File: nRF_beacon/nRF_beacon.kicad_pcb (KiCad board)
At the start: 4 copper layers, 60 x 90 mm, 54 parts, among them J1 Conn_02x05_Odd_Even, J2 Conn_02x03_Counter_Clockwise, U1 nRF54L15-QFAA, U2 NPM1300-QEAA-R7, U3 MAX98357A, U4 12BHC186P1-GR, X1 32MHz, X2 32.768 kHz

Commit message: Done a lot of work, connected all traces
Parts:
- removed NT1, NT2: Net Tie, Ekse:NetTieSmall
- R3, R4: footprint Resistor_SMD:R_0603_1608Metric -> Resistor_SMD:R_0402_1005Metric
- U2: footprint Ekse:QFN32_5X5_NOR -> Ekse:QFN-32_EP_5x5_Pitch0.5mm
- moved J2 81.7 mm to (157.7, 140.8)
- moved J1 81.0 mm to (167.4, 140.5)
- moved D1 19.3 mm to (162.7, 75.1), turned to 90 degrees
- moved R3 15.3 mm to (164.0, 84.2)
- moved R4 15.3 mm to (162.7, 84.2)
- moved FB2 15.2 mm to (156.3, 111.3), turned to 180 degrees
- moved C20 14.0 mm to (159.5, 112.0)
- moved C14 11.7 mm to (158.9, 75.6)
- moved C23 11.3 mm to (157.8, 78.0)
- moved C22 11.3 mm to (161.5, 83.7), turned to 180 degrees
- moved U2 10.9 mm to (162.1, 79.9)
- moved L5 10.9 mm to (155.3, 80.9)
- moved C16 10.9 mm to (155.5, 82.8)
- moved L6 10.9 mm to (155.8, 78.0)
- moved C25 10.9 mm to (167.5, 80.4)
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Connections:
- net Net-(U2-PVDD) renamed /POWER/VSYS
- C14 pad 2: VSS1 -> GND
- C16 pad 2: VSS2 -> GND
- C23 pad 2: VSS1 -> GND
- C24 pad 2: VSS2 -> GND
- FB2 pad 1: Net-(U3-OUTP) -> /AUDIO/OUTP
- FB3 pad 1: Net-(U3-OUTN) -> /AUDIO/OUTN
- U1 pad 39: /MCU/SDA -> /MCU/SCL
- U1 pad 40: /MCU/SCL -> /MCU/SDA
- U2 pad 2: VSS1 -> GND
- U2 pad 6: VSS2 -> GND
- U3 pad 10: Net-(U3-OUTN) -> /AUDIO/OUTN
- U3 pad 9: Net-(U3-OUTP) -> /AUDIO/OUTP
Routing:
- net VDD_AUDIO: track 7.57 -> 112.5 mm, vias 0 -> 2
- net /P1.10: track 1.64 -> 76.8 mm, vias 0 -> 2
- net /P1.09: track 1.54 -> 65.3 mm, vias 0 -> 2
- net VDD_nRF: track 53.4 -> 116.7 mm
- net /P1.13: track 1.53 -> 61.4 mm, vias 0 -> 2
- net /P1.07: track 0.00 -> 56.3 mm, vias 0 -> 2
- net /P1.14: track 1.66 -> 57.8 mm, vias 0 -> 2
- net /VBAT: track 0.00 -> 55.0 mm
- net /P1.08: track 0.00 -> 54.3 mm, vias 0 -> 2
- net /MCU/~{RESET}: track 0.00 -> 45.6 mm
- net /AUDIO/OUTP: track 0.00 -> 41.8 mm
- net /MCU/SWDCLK: track 0.00 -> 40.8 mm
- net /AUDIO/OUTN: track 0.00 -> 38.4 mm
- net /MCU/SWDIO: track 0.00 -> 36.0 mm
- net /BCLK: track 0.00 -> 23.3 mm, vias 0 -> 2
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- added copper zone on B.Cu, net /POWER/VSYS
- added copper zone on F.Cu, net /POWER/VSYS
- added copper zone on B.Cu, net GND
- added copper zone on In1.Cu, net GND
- added copper zone on In2.Cu, net GND
- added copper zone on F.Cu, net VDD_AUDIO

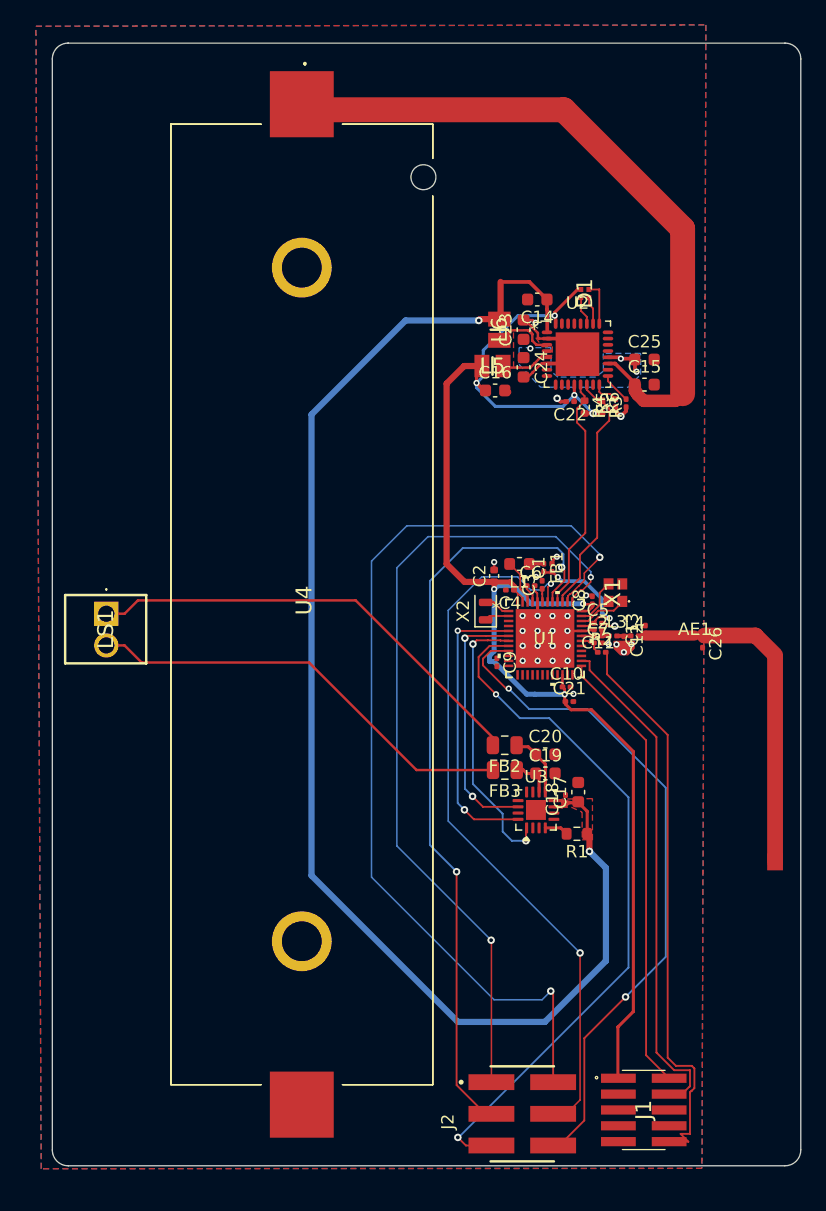
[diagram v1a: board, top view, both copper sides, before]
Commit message: Cleaned up silkscreen
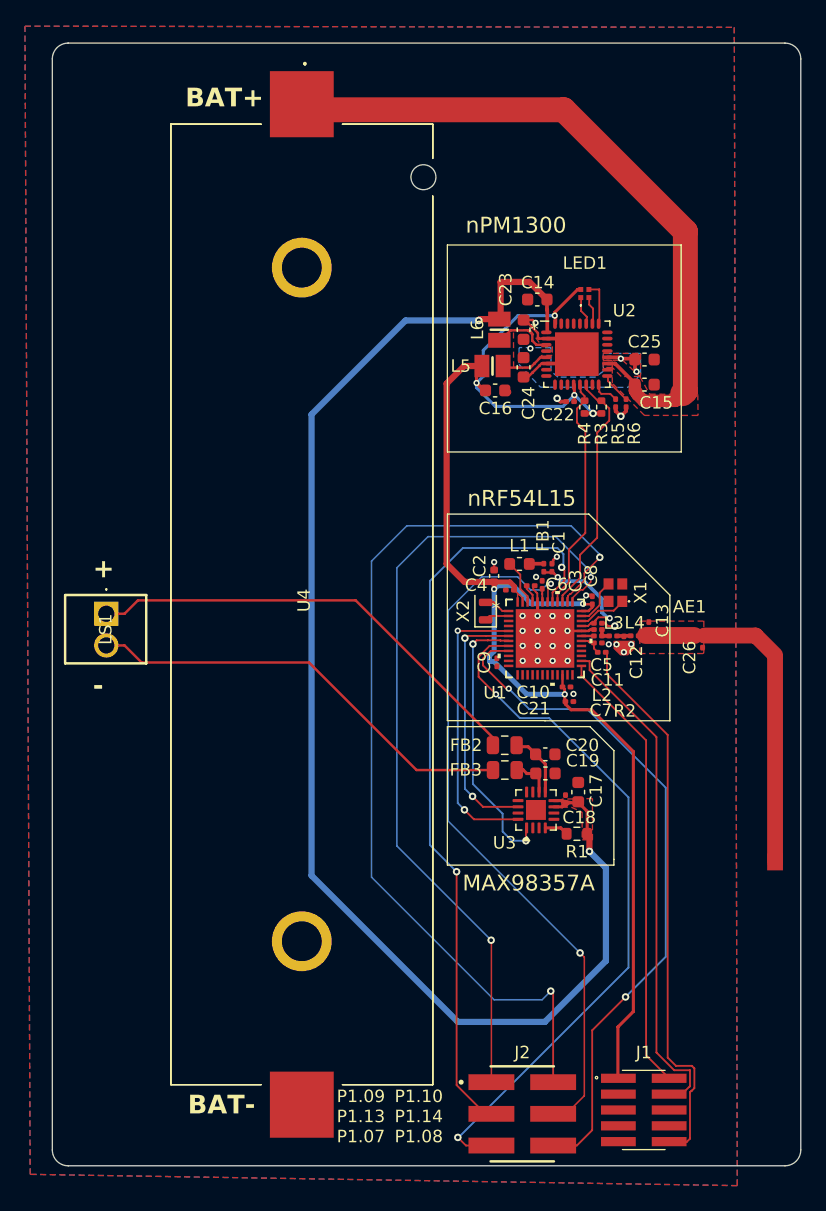
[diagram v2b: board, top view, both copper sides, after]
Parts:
- moved C13 0.40 mm to (167.8, 101.7)
- renumbered D1 to LED1
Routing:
- net /MCU/~{RESET}: track 45.6 -> 44.6 mm
- net /P1.08: track 54.3 -> 55.1 mm
- added copper zone on F.Cu, net /VBAT
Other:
- board text added: "+"
- board text added: "-"
- board text added: "BAT+"
- board text added: "BAT-"
- board text added: "MAX98357A"
- board text added: "P1.09 P1.13 P1.07"
- board text added: "P1.10 P1.14 P1.08"
- board text added: "nPM1300"
- board text added: "nRF54L15"

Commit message: Only 67 DRC errors left
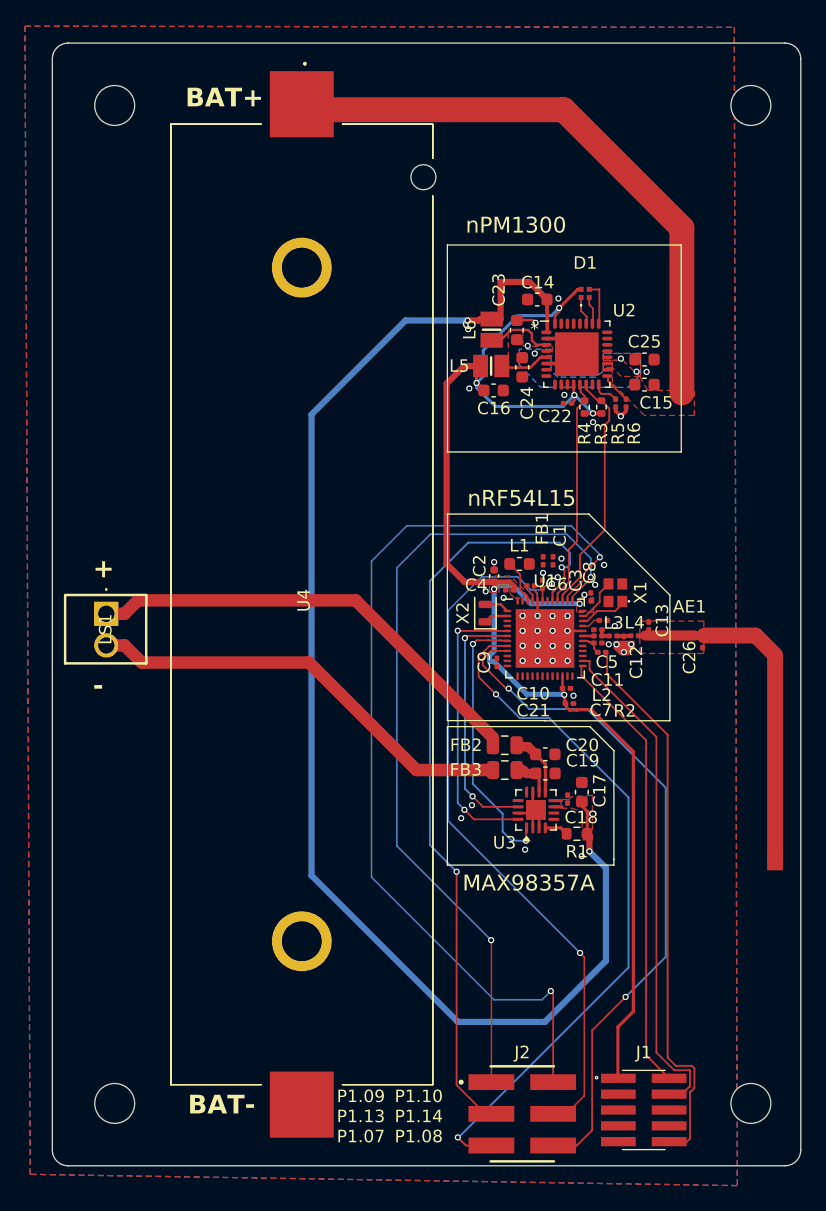
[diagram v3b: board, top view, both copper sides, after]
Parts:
- removed LED1: LED_RGBA, Ekse:APGF1012GBRC07
- added D1: LED_RGBA, Ekse:APGF1012GBRC07, F.Cu at (162.7, 75.1)
- added H1: MountingHole, MountingHole:MountingHole_3.2mm_M3, F.Cu at (125.0, 60.0)
- added H2: MountingHole, MountingHole:MountingHole_3.2mm_M3, F.Cu at (125.0, 140.0)
- added H3: MountingHole, MountingHole:MountingHole_3.2mm_M3, F.Cu at (176.0, 60.0)
- added H4: MountingHole, MountingHole:MountingHole_3.2mm_M3, F.Cu at (176.0, 140.0)
- U1: footprint Ekse:QFN48_6X6_NOR -> Ekse:QFN-48_EP_6x6_Pitch0.4mm
- moved L6 0.62 mm to (155.2, 78.0)
- moved C1 0.56 mm to (160.1, 96.5)
- moved FB1 0.56 mm to (159.3, 96.5)
- moved C23 0.54 mm to (157.2, 78.0)
- moved C5 0.49 mm to (164.2, 101.3)
- moved C8 0.29 mm to (163.2, 99.4)
- moved C17 0.29 mm to (162.4, 115.0)
- moved C22 0.25 mm to (161.3, 83.9)
- moved C18 0.17 mm to (161.3, 115.6)
- moved X2 0.16 mm to (154.7, 100.7)
- moved C21 0.16 mm to (161.4, 107.9)
- moved C16 0.12 mm to (155.4, 82.8)
- moved C10 0.11 mm to (161.2, 106.7)
- moved C24 0.11 mm to (157.7, 81.0)
- moved L5 0.11 mm to (155.2, 80.9)
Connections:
- X1 pad 2: (no net) -> GND
- X1 pad 4: (no net) -> GND
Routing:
- net Net-(U1A-DECA): track 11.1 -> 2.61 mm, vias 2 -> 0
- net /VBAT: track 55.1 -> 47.1 mm
- net GND: track 26.5 -> 23.0 mm, vias 29 -> 44
- net VDD_nRF: track 116.7 -> 113.3 mm
- net /POWER/VSYS: track 3.32 -> 0.21 mm
- net VDD_AUDIO: track 112.5 -> 110.5 mm
- net /P1.13: track 61.4 -> 62.8 mm
- net /P1.14: track 58.1 -> 56.8 mm
- net Net-(U1A-DECD): track 2.68 -> 1.51 mm
- net /P1.09: track 65.3 -> 65.9 mm
- net /MCU/SDA: track 19.0 -> 18.5 mm
- added copper zone on F.Cu, net VDD_nRF

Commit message: Continued fixing DRC errors. Increased trace width on several lines
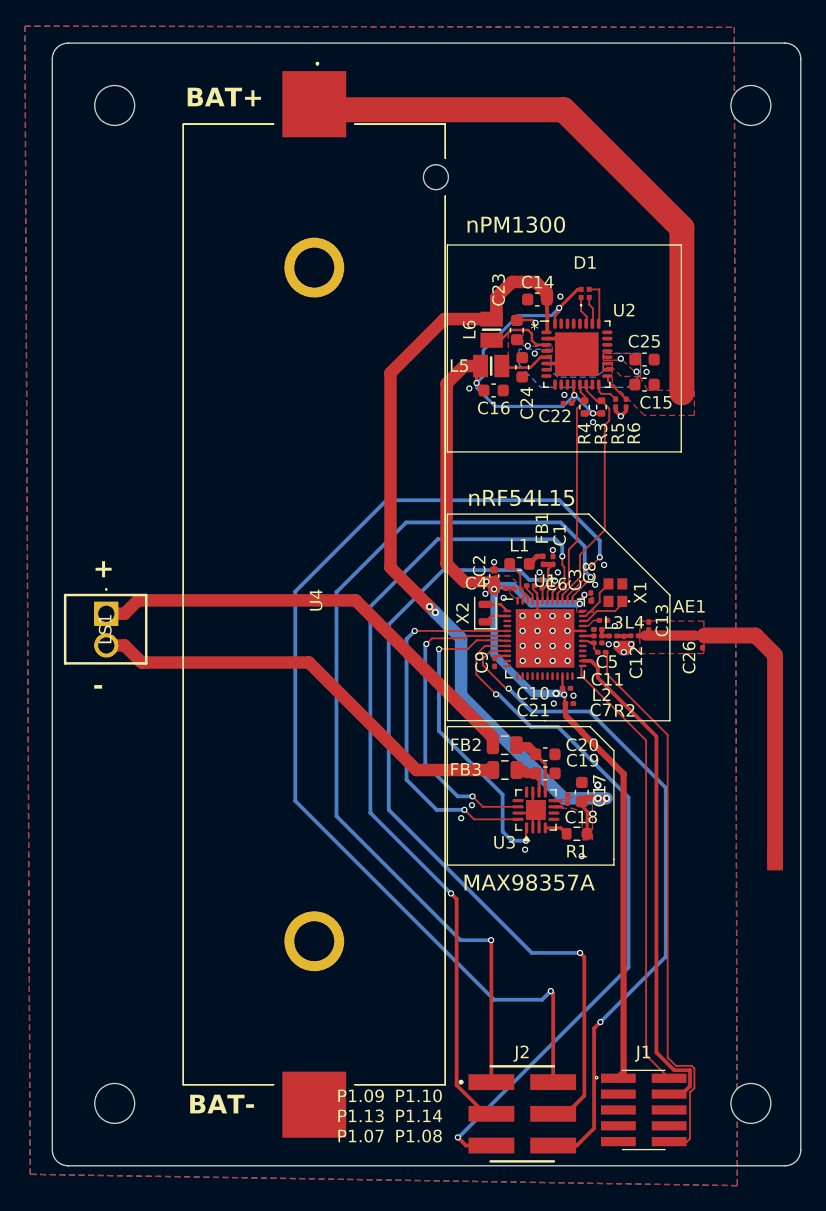
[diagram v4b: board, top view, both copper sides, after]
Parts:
- moved U4 1.00 mm to (141.0, 100.0)
- moved C9 0.18 mm to (155.5, 104.6)
- moved C4 0.12 mm to (156.7, 98.7)
- moved C3 0.06 mm to (159.2, 98.3)
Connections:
- X1 pad 2: GND -> (no net)
- X1 pad 4: GND -> (no net)
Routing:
- net VDD_AUDIO: track 110.5 -> 69.3 mm, vias 2 -> 4
- net /P1.14: track 56.8 -> 67.0 mm
- net /P1.10: track 76.8 -> 86.3 mm
- net /P1.09: track 65.9 -> 74.1 mm
- net /BCLK: track 23.3 -> 30.0 mm
- net /P1.13: track 62.8 -> 67.8 mm
- net /LRCLK: track 20.5 -> 25.4 mm
- net /DIN/DOUT: track 22.2 -> 25.8 mm
- net VDD_nRF: track 113.3 -> 110.1 mm, vias 7 -> 9
- net Net-(U1A-DECA): track 2.61 -> 5.73 mm
- net Net-(U1A-DECD): track 1.51 -> 2.87 mm
- net GND: vias 44 -> 45

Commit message: Adjustments to GPIO connector. Added testpads. Polygon pour by antenna for correct impedance matching
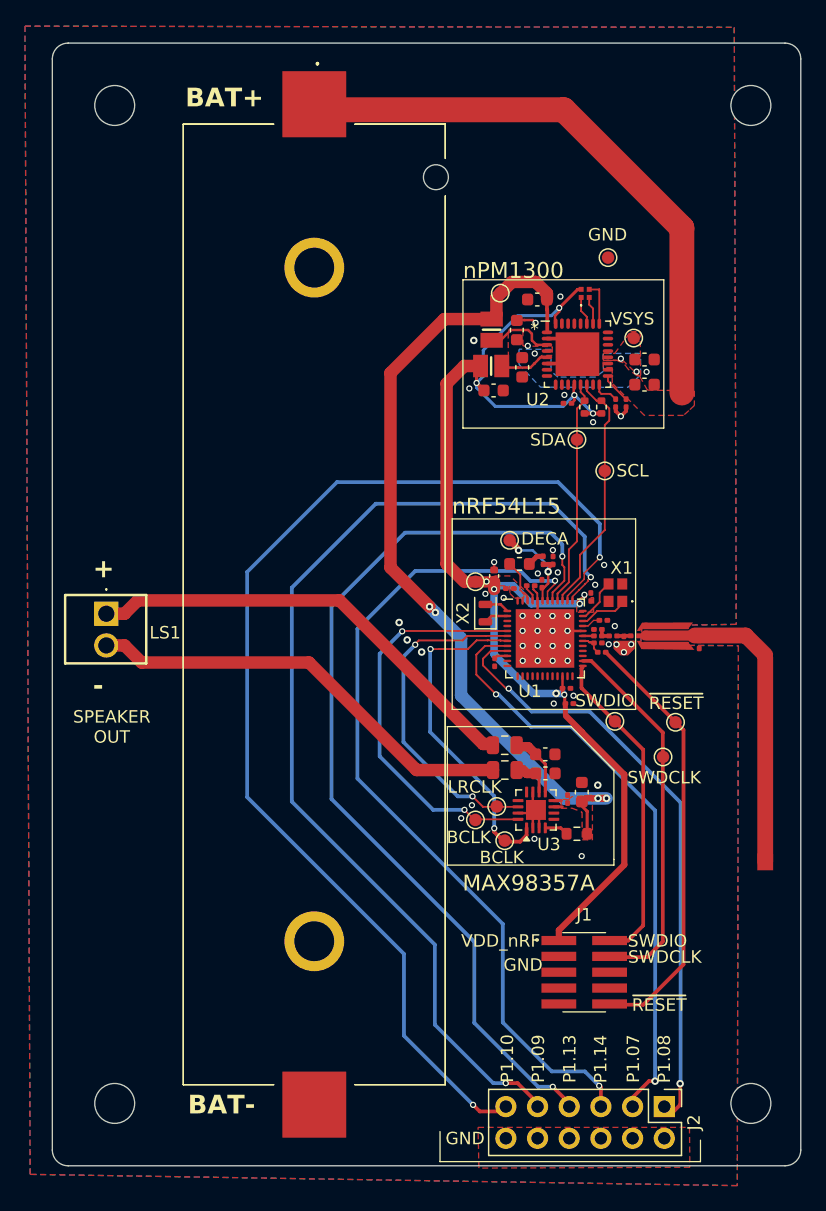
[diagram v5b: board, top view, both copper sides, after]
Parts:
- added TP1: VDD_nRF, TestPoint:TestPoint_Pad_D1.0mm, F.Cu at (153.9, 98.2)
- added TP10: VDD_AUDIO, TestPoint:TestPoint_Pad_D1.0mm, F.Cu at (155.9, 75.0)
- added TP11: SDA, TestPoint:TestPoint_Pad_D1.0mm, F.Cu at (162.1, 86.8)
- added TP12: SCL, TestPoint:TestPoint_Pad_D1.0mm, F.Cu at (164.3, 89.3)
- added TP13: BCLK, TestPoint:TestPoint_Pad_D1.0mm, F.Cu at (153.9, 117.3)
- added TP14: DOUT, TestPoint:TestPoint_Pad_D1.0mm, F.Cu at (156.3, 118.9)
- added TP15: LRCLK, TestPoint:TestPoint_Pad_D1.0mm, F.Cu at (155.6, 116.2)
- added TP3: DECA, TestPoint:TestPoint_Pad_D1.0mm, F.Cu at (156.7, 94.9)
- added TP4: SWDIO, TestPoint:TestPoint_Pad_D1.0mm, F.Cu at (165.1, 109.4)
- added TP5: SWDCLK, TestPoint:TestPoint_Pad_D1.0mm, F.Cu at (169.0, 112.2)
- added TP6: ~{RESET}, TestPoint:TestPoint_Pad_D1.0mm, F.Cu at (170.0, 109.4)
- added TP8: VSYS, TestPoint:TestPoint_Pad_D1.0mm, F.Cu at (166.6, 78.6)
- added TP9: GND, TestPoint:TestPoint_Pad_D1.0mm, F.Cu at (164.5, 72.2)
- J2: footprint Ekse:SAMTEC_TSM-103-01-L-DV-P-TR -> Connector_PinHeader_2.54mm:PinHeader_2x06_P2.54mm_Vertical
- moved J1 12.0 mm to (162.6, 129.5)
- moved J2 11.4 mm to (169.1, 140.3), turned to -90 degrees
- moved C13 0.36 mm to (167.6, 102.0)
- moved C26 0.27 mm to (171.9, 103.2)
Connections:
- J2 pad 1: /P1.09 -> /P1.07
- J2 pad 2: /P1.10 -> /P1.08
- J2 pad 3: /P1.13 -> /P1.09
- J2 pad 4: /P1.14 -> /P1.10
- J2 pad 5: /P1.07 -> /P1.13
- J2 pad 6: /P1.08 -> /P1.14
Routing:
- net /MCU/SWDCLK: track 40.7 -> 29.7 mm
- net /P1.09: track 74.1 -> 84.7 mm
- net /MCU/~{RESET}: track 44.6 -> 34.2 mm
- net /MCU/SWDIO: track 36.0 -> 26.0 mm
- net VDD_nRF: track 110.1 -> 101.1 mm
- net /P1.07: track 56.7 -> 48.5 mm
- net /P1.13: track 67.8 -> 75.5 mm
- net /P1.10: track 86.3 -> 93.1 mm
- net /P1.08: track 55.1 -> 49.0 mm
- net Net-(U1A-DECA): track 5.73 -> 10.2 mm, vias 0 -> 2
- net /BCLK: track 30.0 -> 32.5 mm
- net /LRCLK: track 25.4 -> 27.3 mm
- net /P1.14: track 67.0 -> 68.4 mm
- net /DIN/DOUT: track 25.8 -> 27.1 mm
- net GND: vias 45 -> 49
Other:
- board text added: "BCLK"
- board text added: "DECA"
- board text added: "GND"
- board text added: "LRCLK"
- board text added: "P1.07"
- board text added: "P1.08"
- board text added: "P1.09"
- board text added: "P1.10"
- board text added: "P1.13"
- board text added: "P1.14"
- board text added: "SCL"
- board text added: "SDA"
- board text added: "SPEAKER OUT"
- board text added: "SWDCLK"
- board text added: "SWDIO"
- board text added: "VDD_nRF"
- board text added: "VSYS"
- board text added: "~{RESET}"
- board text removed: "P1.09 P1.13 P1.07"
- board text removed: "P1.10 P1.14 P1.08"

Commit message: Added stitching vias and completed DRC tests
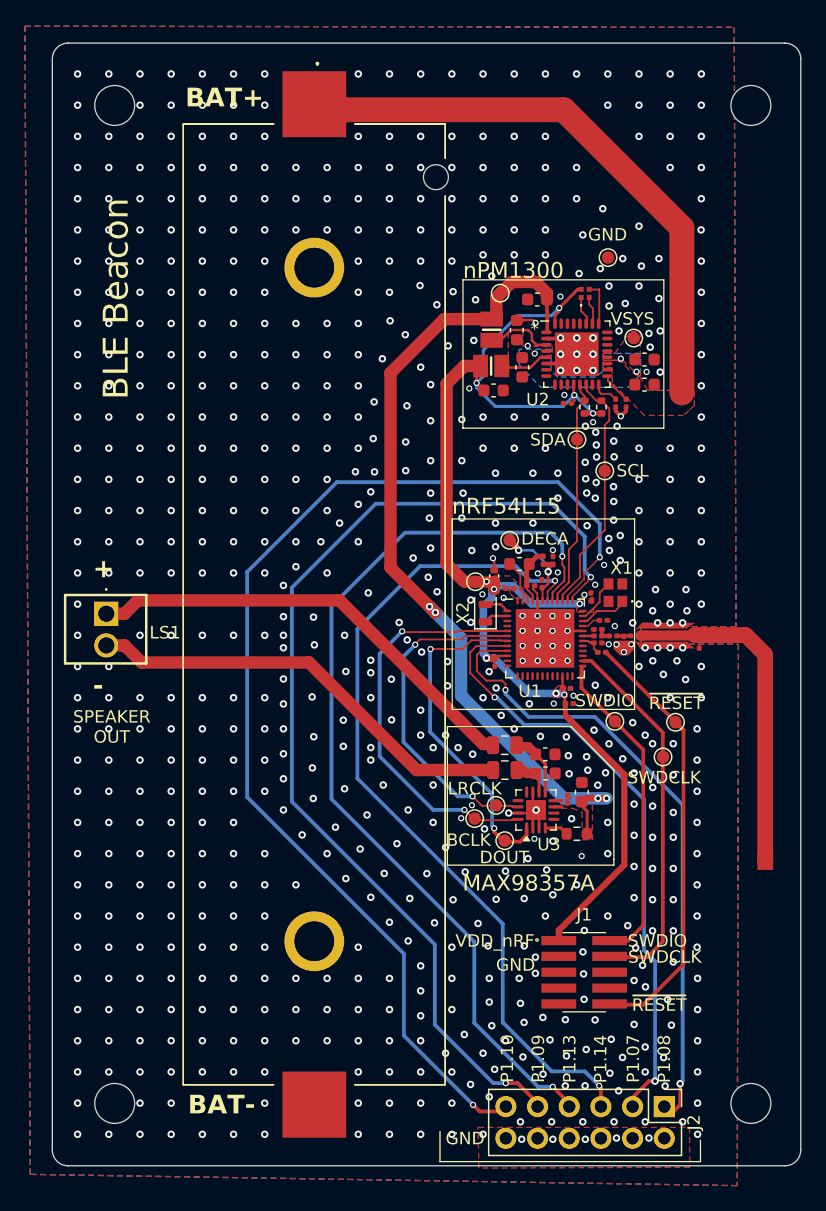
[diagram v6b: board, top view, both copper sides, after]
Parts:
- moved TP13 0.12 mm to (153.9, 117.2)
- moved TP15 0.10 mm to (155.6, 116.1)
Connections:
- X1 pad 2: (no net) -> GND
- X1 pad 4: (no net) -> GND
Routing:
- net /P1.08: track 49.0 -> 51.0 mm
- net VDD_nRF: track 101.1 -> 103.0 mm, vias 9 -> 10
- net Net-(U1A-DECD): track 2.87 -> 4.70 mm
- net GND: track 23.0 -> 21.3 mm, vias 49 -> 730
- net /P1.07: track 48.5 -> 49.5 mm
- net VDD_AUDIO: track 69.3 -> 70.0 mm
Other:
- board text added: "BLE Beacon"
- board text added: "DOUT"
- board text added: "Rev A"
